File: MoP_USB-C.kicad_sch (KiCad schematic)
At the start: 14 parts, among them J21 USB4105-GF-A, U16 FT230XS

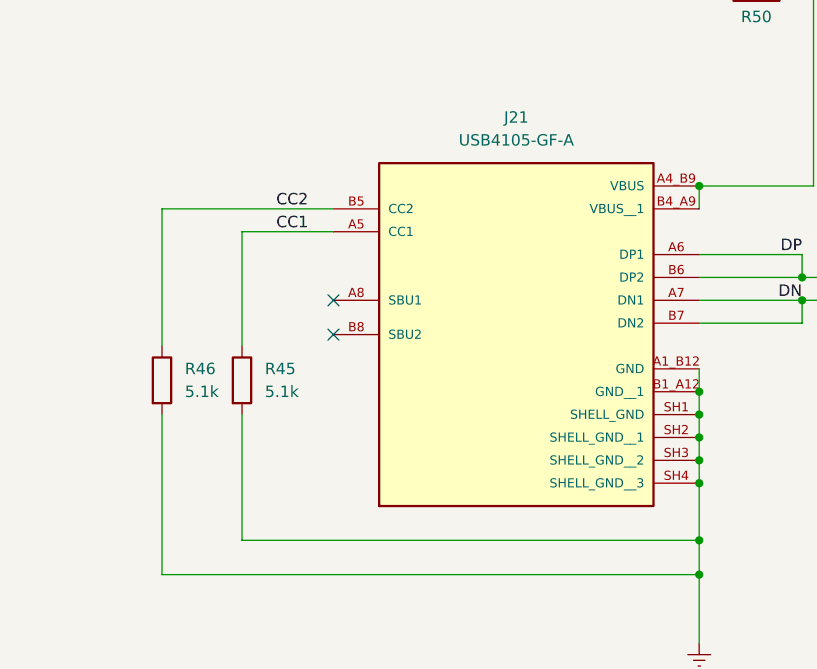
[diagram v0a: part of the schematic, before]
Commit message: changed ref designators to be consistent accross sheets
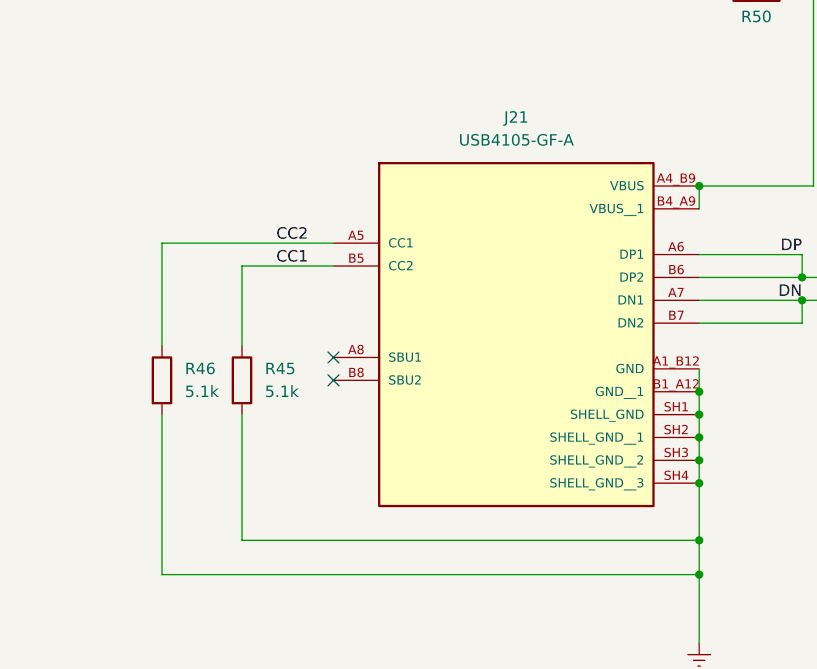
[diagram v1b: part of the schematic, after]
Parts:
- C34, C35: footprint (none) -> Capacitor_SMD:C_0805_2012Metric_Pad1.18x1.45mm_HandSolder
- D5, D6: footprint (none) -> LED_SMD:LED_0805_2012Metric
- J21: footprint USB4105-GF-A:GCT_USB4105-GF-A -> Nigels_Library:GCT_USB4105-GF-A
- R44, R45, R46, R47, R48, R50: footprint (none) -> Resistor_SMD:R_0805_2012Metric
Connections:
- net CC1: now also J21.B5 (CC2); no longer J21.A5 (CC1)
- net CC2: now also J21.A5 (CC1); no longer J21.B5 (CC2)
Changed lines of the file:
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@@
 	)
 	(no_connect
-		(at 81.28 107.95)
+		(at 81.28 114.3)
 	)
 	(no_connect
@@
 	)
 	(no_connect
-		(at 81.28 111.76)
+		(at 81.28 116.84)
 	)
 	(bus_entry
@@
 	(wire
 		(pts
-			(xy 71.12 100.33) (xy 71.12 113.03)
+			(xy 71.12 104.14) (xy 71.12 113.03)
 		)
 		(stroke
@@
 	(wire
 		(pts
-			(xy 81.28 100.33) (xy 71.12 100.33)
+			(xy 81.28 104.14) (xy 71.12 104.14)
 		)
 		(stroke
@@
 	(wire
 		(pts
-			(xy 81.28 97.79) (xy 62.23 97.79)
+			(xy 81.28 101.6) (xy 62.23 101.6)
 		)
 		(stroke
@@
 	(wire
 		(pts
-			(xy 62.23 97.79) (xy 62.23 113.03)
+			(xy 62.23 101.6) (xy 62.23 113.03)
 		)
 		(stroke
@@
 	)
 	(label "CC2"
-		(at 74.93 97.79 0)
+		(at 74.93 101.6 0)
 		(fields_autoplaced yes)
 		(effects
@@
 	)
 	(label "CC1"
-		(at 74.93 100.33 0)
+		(at 74.93 104.14 0)
 		(fields_autoplaced yes)
 		(effects
@@
 			)
 		)
-		(property "Footprint" ""
+		(property "Footprint" "LED_SMD:LED_0805_2012Metric"
 			(at 215.9 110.49 0)
 			(effects
@@
 			)
 		)
-		(property "Footprint" "USB4105-GF-A:GCT_USB4105-GF-A"
+		(property "Footprint" "Nigels_Library:GCT_USB4105-GF-A"
 			(at 101.092 78.994 0)
 			(effects
@@
 			)
 		)
-		(property "Footprint" ""
+		(property "Footprint" "Resistor_SMD:R_0805_2012Metric"
 			(at 60.452 116.84 90)
 			(effects
@@
 			)
 		)
-		(property "Footprint" ""
+		(property "Footprint" "Resistor_SMD:R_0805_2012Metric"
 			(at 128.27 75.438 90)
 			(effects
@@
 			)
 		)
-		(property "Footprint" ""
+		(property "Footprint" "Resistor_SMD:R_0805_2012Metric"
 			(at 69.342 116.84 90)
 			(effects
@@
 			)
 		)
-		(property "Footprint" ""
+		(property "Footprint" "Resistor_SMD:R_0805_2012Metric"
 			(at 228.6 119.888 90)
 			(effects
@@
 			)
 		)
-		(property "Footprint" ""
+		(property "Footprint" "LED_SMD:LED_0805_2012Metric"
 			(at 215.9 118.11 0)
 			(effects
@@
 			)
 		)
-		(property "Footprint" ""
+		(property "Footprint" "Resistor_SMD:R_0805_2012Metric"
 			(at 228.6 112.268 90)
 			(effects
@@
 			)
 		)
-		(property "Footprint" ""
+		(property "Footprint" "Resistor_SMD:R_0805_2012Metric"
 			(at 128.27 64.008 90)
 			(effects
@@
 			)
 		)
-		(property "Footprint" ""
+		(property "Footprint" "Capacitor_SMD:C_0805_2012Metric_Pad1.18x1.45mm_HandSolder"
 			(at 159.7152 82.55 0)
 			(effects
@@
 			)
 		)
-		(property "Footprint" ""
+		(property "Footprint" "Capacitor_SMD:C_0805_2012Metric_Pad1.18x1.45mm_HandSolder"
 			(at 149.5552 82.55 0)
 			(effects

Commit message: Finished schematics
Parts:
- JP601: renamed from JP12; footprint (none) -> Connector_PinHeader_2.54mm:PinHeader_1x02_P2.54mm_Vertical
- JP602: renamed from JP13; footprint (none) -> Connector_PinHeader_2.54mm:PinHeader_1x02_P2.54mm_Vertical
- R601: renamed from R44; now not fitted
- R602: renamed from R50; now not fitted
- renumbered C35 to C601, C34 to C602, D5 to D601, D6 to D602, R46 to R603, R45 to R604, R47 to R605, R48 to R606
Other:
- moved on the sheet: D602, R606
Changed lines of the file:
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@@
 	(wire
 		(pts
-			(xy 219.71 118.11) (xy 224.79 118.11)
-		)
-		(stroke
-			(width 0)
-			(type default)
-		)
-	)
-	(wire
-		(pts
-			(xy 237.49 110.49) (xy 237.49 118.11)
+			(xy 219.71 119.38) (xy 224.79 119.38)
+		)
+		(stroke
+			(width 0)
+			(type default)
+		)
+	)
+	(wire
+		(pts
+			(xy 237.49 110.49) (xy 237.49 119.38)
 		)
 		(stroke
@@
 	(wire
 		(pts
-			(xy 209.55 118.11) (xy 212.09 118.11)
+			(xy 209.55 119.38) (xy 212.09 119.38)
 		)
 		(stroke
@@
 	(wire
 		(pts
-			(xy 237.49 118.11) (xy 232.41 118.11)
+			(xy 237.49 119.38) (xy 232.41 119.38)
 		)
 		(stroke
@@
 	(wire
 		(pts
-			(xy 209.55 113.03) (xy 209.55 118.11)
+			(xy 209.55 113.03) (xy 209.55 119.38)
 		)
 		(stroke
@@
 	(wire
 		(pts
-			(xy 134.62 58.42) (xy 134.62 62.23)
+			(xy 134.62 62.23) (xy 134.62 58.42)
 		)
 		(stroke
@@
 		(on_board yes)
 		(dnp no)
-		(property "Reference" "D5"
+		(property "Reference" "D601"
 			(at 215.9 107.696 0)
 			(effects
@@
 			(project ""
 				(path "/4d76798e-9a11-4d8d-a723-72f274a89091/63f46eb8-407d-4e29-86cd-16d2149e2636"
-					(reference "D5")
+					(reference "D601")
 					(unit 1)
 				)
@@
 		(dnp no)
 		(fields_autoplaced yes)
-		(property "Reference" "JP13"
+		(property "Reference" "JP602"
 			(at 128.27 67.31 0)
 			(effects
@@
 			)
 		)
-		(property "Footprint" ""
+		(property "Footprint" "Connector_PinHeader_2.54mm:PinHeader_1x02_P2.54mm_Vertical"
 			(at 128.27 69.85 0)
 			(effects
@@
 			(project "MoP"
 				(path "/4d76798e-9a11-4d8d-a723-72f274a89091/63f46eb8-407d-4e29-86cd-16d2149e2636"
-					(reference "JP13")
+					(reference "JP602")
 					(unit 1)
 				)
@@
 		(dnp no)
 		(fields_autoplaced yes)
-		(property "Reference" "R46"
+		(property "Reference" "R603"
 			(at 64.77 115.5699 0)
 			(effects
@@
 			(project "MoP"
 				(path "/4d76798e-9a11-4d8d-a723-72f274a89091/63f46eb8-407d-4e29-86cd-16d2149e2636"
-					(reference "R46")
+					(reference "R603")
 					(unit 1)
 				)
@@
 		(dnp no)
 		(fields_autoplaced yes)
-		(property "Reference" "JP12"
+		(property "Reference" "JP601"
 			(at 128.27 55.88 0)
 			(effects
@@
 			)
 		)
-		(property "Footprint" ""
+		(property "Footprint" "Connector_PinHeader_2.54mm:PinHeader_1x02_P2.54mm_Vertical"
 			(at 128.27 58.42 0)
 			(effects
@@
 			(project "MoP"
 				(path "/4d76798e-9a11-4d8d-a723-72f274a89091/63f46eb8-407d-4e29-86cd-16d2149e2636"
-					(reference "JP12")
+					(reference "JP601")
 					(unit 1)
 				)
@@
 		(exclude_from_sim no)
 		(in_bom yes)
-		(on_board yes)
-		(dnp no)
-		(property "Reference" "R50"
+		(on_board no)
+		(dnp yes)
+		(property "Reference" "R602"
 			(at 128.27 76.454 90)
 			(effects
@@
 			(project "MoP"
 				(path "/4d76798e-9a11-4d8d-a723-72f274a89091/63f46eb8-407d-4e29-86cd-16d2149e2636"
-					(reference "R50")
+					(reference "R602")
 					(unit 1)
 				)
@@
 		(dnp no)
 		(fields_autoplaced yes)
-		(property "Reference" "R45"
+		(property "Reference" "R604"
 			(at 73.66 115.5699 0)
 			(effects
@@
 			(project ""
 				(path "/4d76798e-9a11-4d8d-a723-72f274a89091/63f46eb8-407d-4e29-86cd-16d2149e2636"
-					(reference "R45")
+					(reference "R604")
 					(unit 1)
 				)
@@
 	(symbol
 		(lib_id "Device:R")
-		(at 228.6 118.11 90)
+		(at 228.6 119.38 90)
 		(unit 1)
 		(exclude_from_sim no)
@@
 		(on_board yes)
 		(dnp no)
-		(property "Reference" "R48"
-			(at 228.6 115.824 90)
+		(property "Reference" "R606"
+			(at 228.6 117.094 90)
 			(effects
 				(font
@@
 		)
 		(property "Value" "470"
-			(at 228.6 120.904 90)
+			(at 228.6 122.174 90)
 			(effects
 				(font
@@
 		)
 		(property "Footprint" "Resistor_SMD:R_0805_2012Metric"
-			(at 228.6 119.888 90)
+			(at 228.6 121.158 90)
 			(effects
 				(font
@@
 		)
 		(property "Datasheet" "~"
-			(at 228.6 118.11 0)
+			(at 228.6 119.38 0)
 			(effects
 				(font
@@
 		)
 		(property "Description" "Resistor"
-			(at 228.6 118.11 0)
+			(at 228.6 119.38 0)
 			(effects
 				(font
@@
 			(project "MoP"
 				(path "/4d76798e-9a11-4d8d-a723-72f274a89091/63f46eb8-407d-4e29-86cd-16d2149e2636"
-					(reference "R48")
+					(reference "R606")
 					(unit 1)
 				)
@@
 	(symbol
 		(lib_id "Device:LED")
-		(at 215.9 118.11 0)
+		(at 215.9 119.38 0)
 		(unit 1)
 		(exclude_from_sim no)
@@
 		(on_board yes)
 		(dnp no)
-		(property "Reference" "D6"
-			(at 215.9 115.316 0)
+		(property "Reference" "D602"
+			(at 215.9 116.586 0)
 			(effects
 				(font
@@
 		)
 		(property "Value" "LED"
-			(at 216.154 121.412 0)
+			(at 216.154 122.682 0)
 			(effects
 				(font
@@
 		)
 		(property "Footprint" "LED_SMD:LED_0805_2012Metric"
-			(at 215.9 118.11 0)
+			(at 215.9 119.38 0)
 			(effects
 				(font
@@
 		)
 		(property "Datasheet" "~"
-			(at 215.9 118.11 0)
+			(at 215.9 119.38 0)
 			(effects
 				(font
@@
 		)
 		(property "Description" "Light emitting diode"
-			(at 215.9 118.11 0)
+			(at 215.9 119.38 0)
 			(effects
 				(font
@@
 			(project "MoP"
 				(path "/4d76798e-9a11-4d8d-a723-72f274a89091/63f46eb8-407d-4e29-86cd-16d2149e2636"
-					(reference "D6")
+					(reference "D602")
 					(unit 1)
 				)
@@
 		(on_board yes)
 		(dnp no)
-		(property "Reference" "R47"
+		(property "Reference" "R605"
 			(at 228.6 107.95 90)
 			(effects
@@
 			(project ""
 				(path "/4d76798e-9a11-4d8d-a723-72f274a89091/63f46eb8-407d-4e29-86cd-16d2149e2636"
-					(reference "R47")
+					(reference "R605")
 					(unit 1)
 				)
@@
 		(exclude_from_sim no)
 		(in_bom yes)
-		(on_board yes)
-		(dnp no)
-		(property "Reference" "R44"
+		(on_board no)
+		(dnp yes)
+		(property "Reference" "R601"
 			(at 128.27 65.024 90)
 			(effects
@@
 			(project "MoP"
 				(path "/4d76798e-9a11-4d8d-a723-72f274a89091/63f46eb8-407d-4e29-86cd-16d2149e2636"
-					(reference "R44")
+					(reference "R601")
 					(unit 1)
 				)
@@
 		(on_board yes)
 		(dnp no)
-		(fields_autoplaced yes)
-		(property "Reference" "C34"
-			(at 162.56 77.4699 0)
+		(property "Reference" "C602"
+			(at 161.29 75.946 0)
 			(effects
 				(font
@@
 		)
 		(property "Value" "C"
-			(at 162.56 80.0099 0)
+			(at 161.544 81.788 0)
 			(effects
 				(font
@@
 			(project ""
 				(path "/4d76798e-9a11-4d8d-a723-72f274a89091/63f46eb8-407d-4e29-86cd-16d2149e2636"
-					(reference "C34")
+					(reference "C602")
 					(unit 1)
 				)
@@
 		(on_board yes)
 		(dnp no)
-		(fields_autoplaced yes)
-		(property "Reference" "C35"
-			(at 152.4 77.4699 0)
+		(property "Reference" "C601"
+			(at 150.368 75.692 0)
 			(effects
 				(font
@@
 		)
 		(property "Value" "C"
-			(at 152.4 80.0099 0)
+			(at 150.114 81.788 0)
 			(effects
 				(font
@@
 			(project "MoP"
 				(path "/4d76798e-9a11-4d8d-a723-72f274a89091/63f46eb8-407d-4e29-86cd-16d2149e2636"
-					(reference "C35")
+					(reference "C601")
 					(unit 1)
 				)

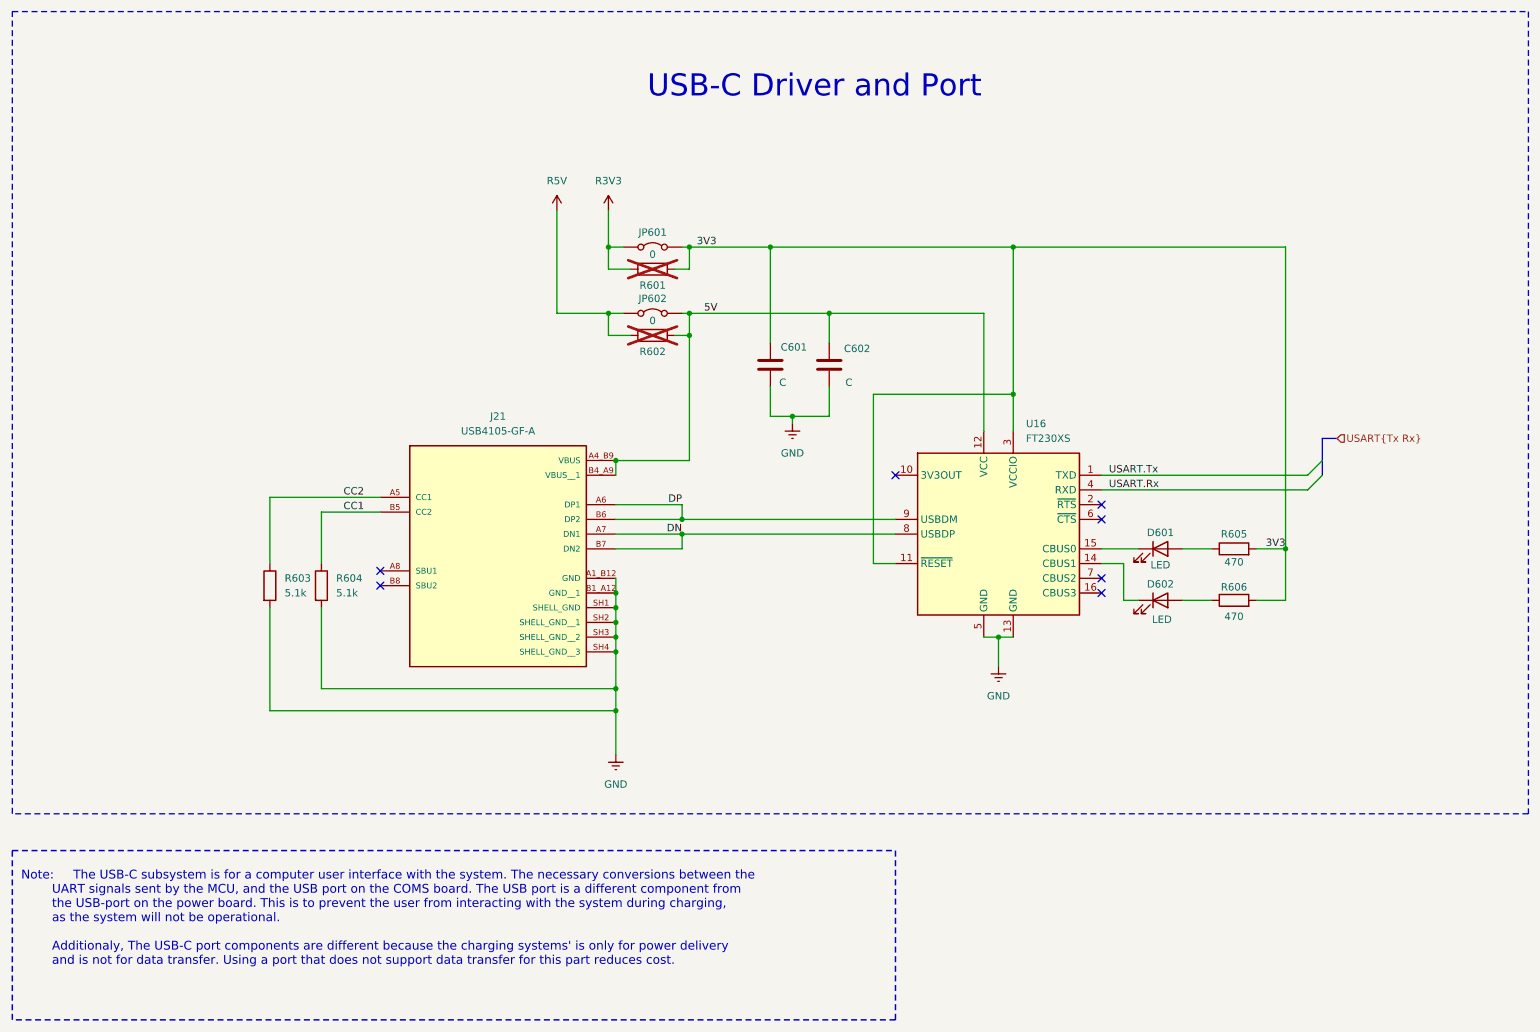
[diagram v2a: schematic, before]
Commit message: Added subproject for EPS PCB
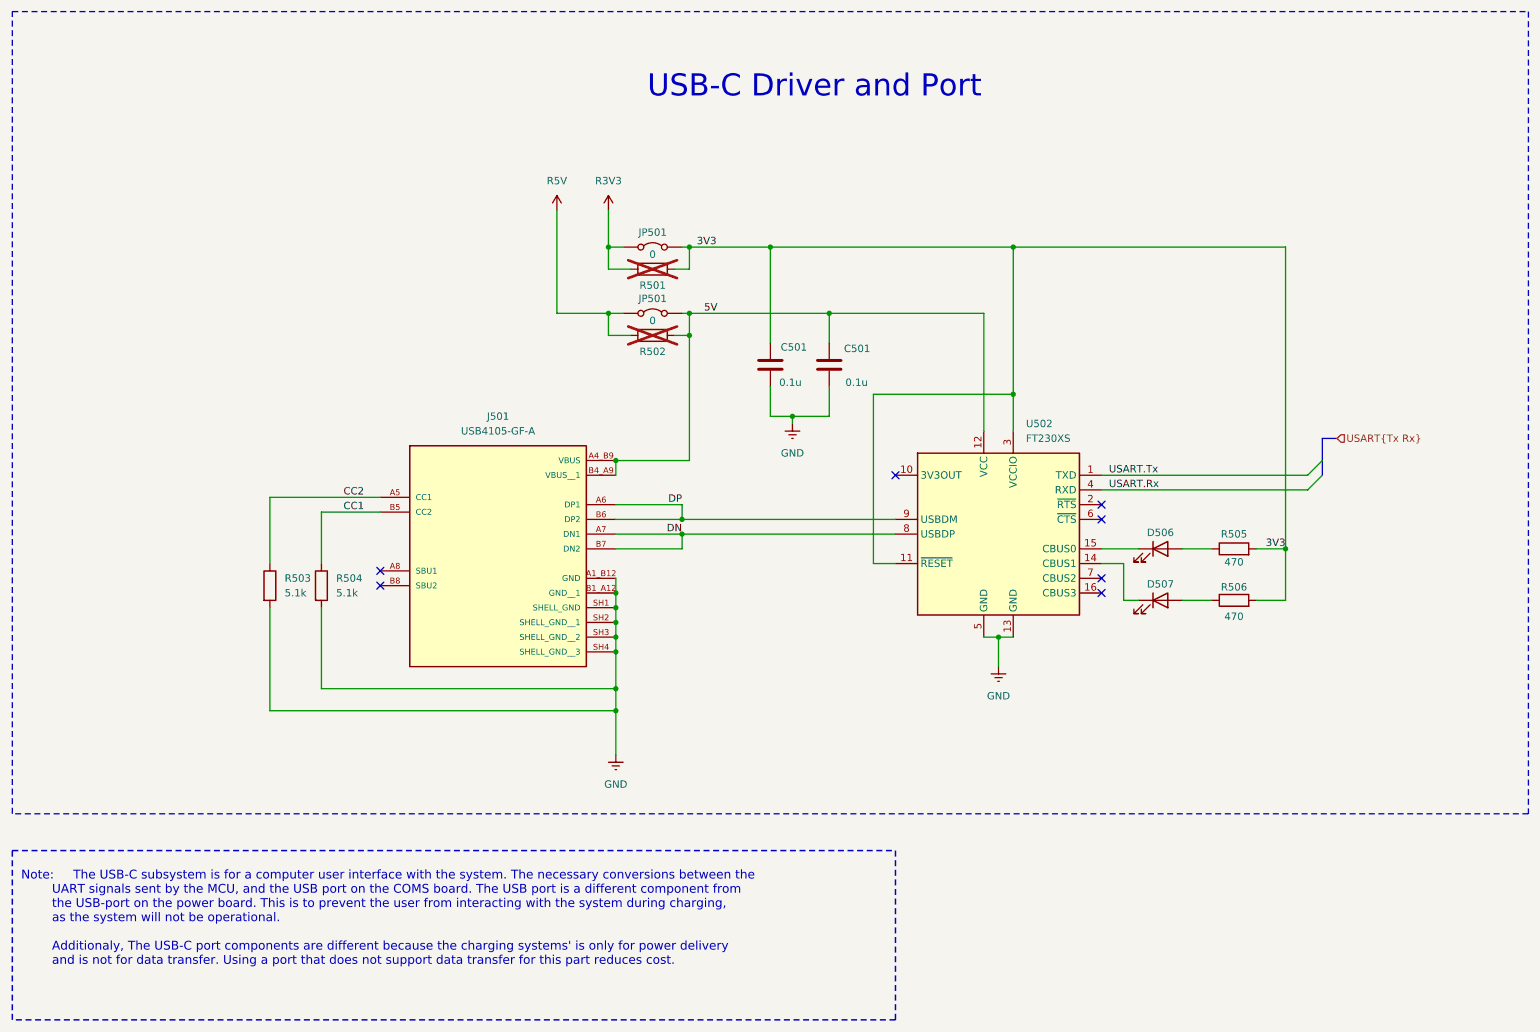
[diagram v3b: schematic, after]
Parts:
- C501: renamed from C602; value C -> 0.1u
- C501: renamed from C601; value C -> 0.1u
- D506: renamed from D601; value LED -> CMD17-21VGC/TR8
- D507: renamed from D602; value LED -> CMD17-21VGC/TR8
- renumbered J21 to J501, JP602 to JP501, JP601 to JP501, R601 to R501, R602 to R502, R603 to R503, R604 to R504, R605 to R505, R606 to R506, U16 to U502
